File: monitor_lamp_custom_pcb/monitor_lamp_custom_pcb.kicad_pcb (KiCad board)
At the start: 2 copper layers, 50 x 35 mm, 32 parts, among them IC1 HUSB238, J1 USB_C_Receptacle_PowerOnly_6P, J2 VEML7700_Connection, J3 LD2410C_Connection, J4 Conn_01x02, J5 Conn_01x01, J7 Conn_01x01, J8 Conn_01x01, J9 Conn_01x01, Q1 AO3401A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

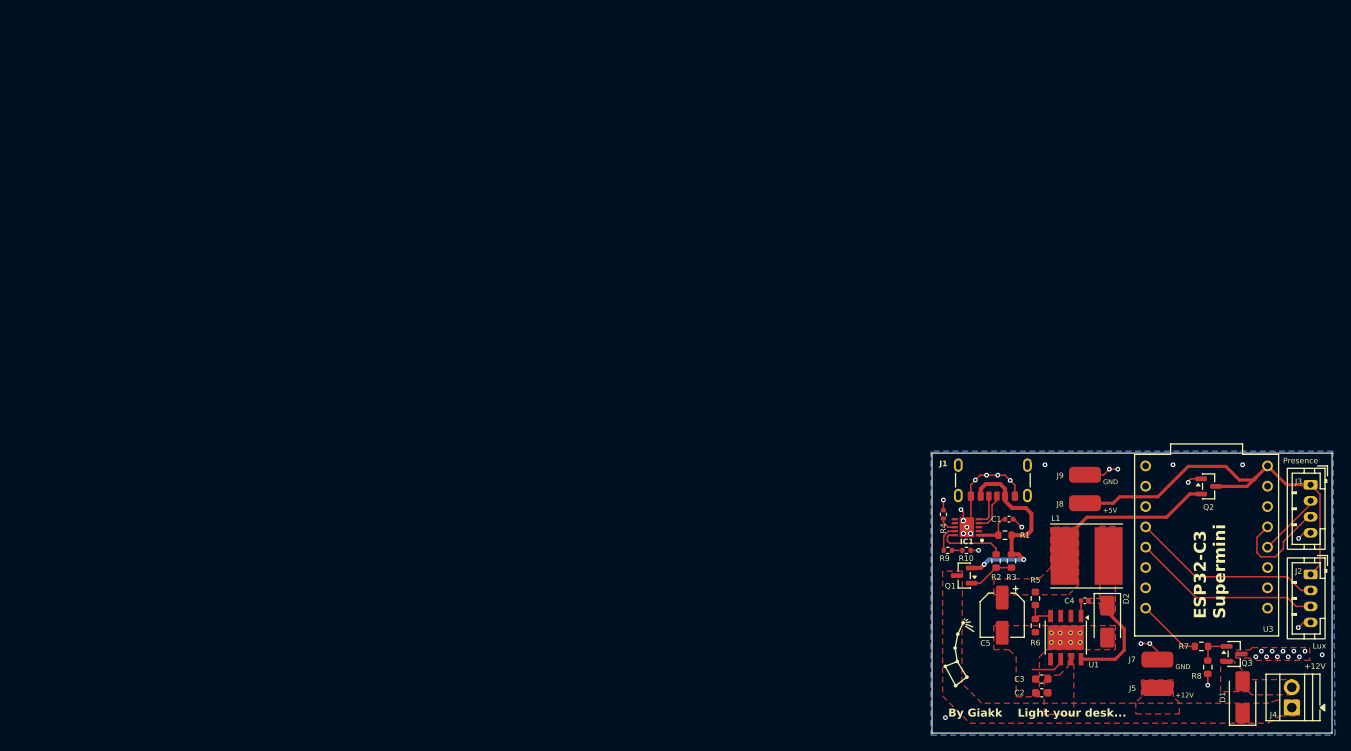
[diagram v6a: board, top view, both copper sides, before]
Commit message: Corrected ISET pin error and changed to pads for connecting LED supply
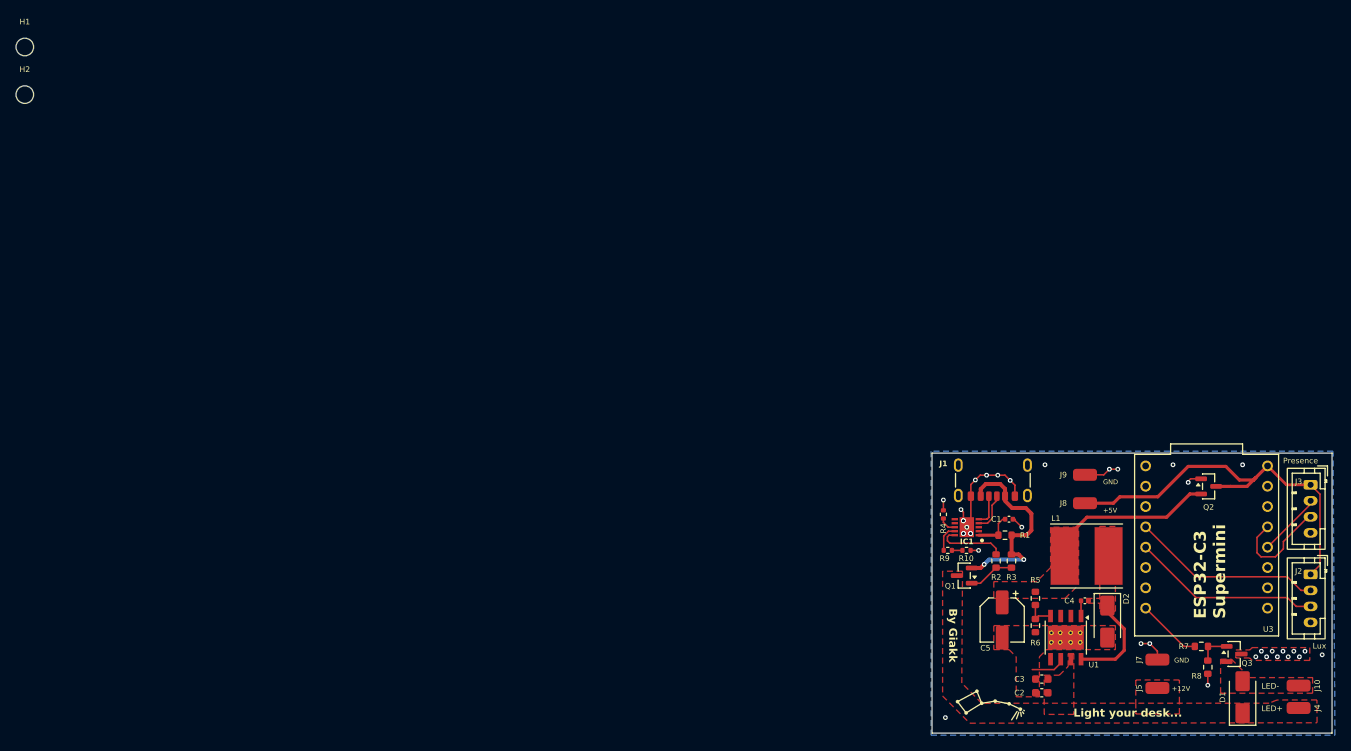
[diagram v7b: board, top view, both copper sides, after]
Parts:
- added H1: MountingHole, MountingHole:MountingHole_2.2mm_M2, F.Cu at (2.48, 2.48)
- added H2: MountingHole, MountingHole:MountingHole_2.2mm_M2, F.Cu at (2.48, 8.43)
- added J10: Conn_01x01, Connector_Wire:SolderWirePad_1x01_SMD_1.5x3mm, F.Cu at (161.7, 82.3)
- J4: value Conn_01x02 -> Conn_01x01; footprint TerminalBlock:TerminalBlock_Xinya_XY308-2.54-2P_1x02_P2.54mm_Horizontal -> Connector_Wire:SolderWirePad_1x01_SMD_1.5x3mm
- J5, J7, J8, J9: footprint Connector_Wire:SolderWirePad_1x01_SMD_2x4mm -> Connector_Wire:SolderWirePad_1x01_SMD_1.5x3mm
- moved J4 0.85 mm to (161.7, 85.1)
- moved C5 0.60 mm to (124.7, 74.1)
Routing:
- net GND: track 38.0 -> 34.4 mm, vias 38 -> 36
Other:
- board text added: "By Giakk"
- board text added: "LED+"
- board text added: "LED-"
- board text added: "Light your desk..."
- board text removed: "By Giakk Light your desk..."

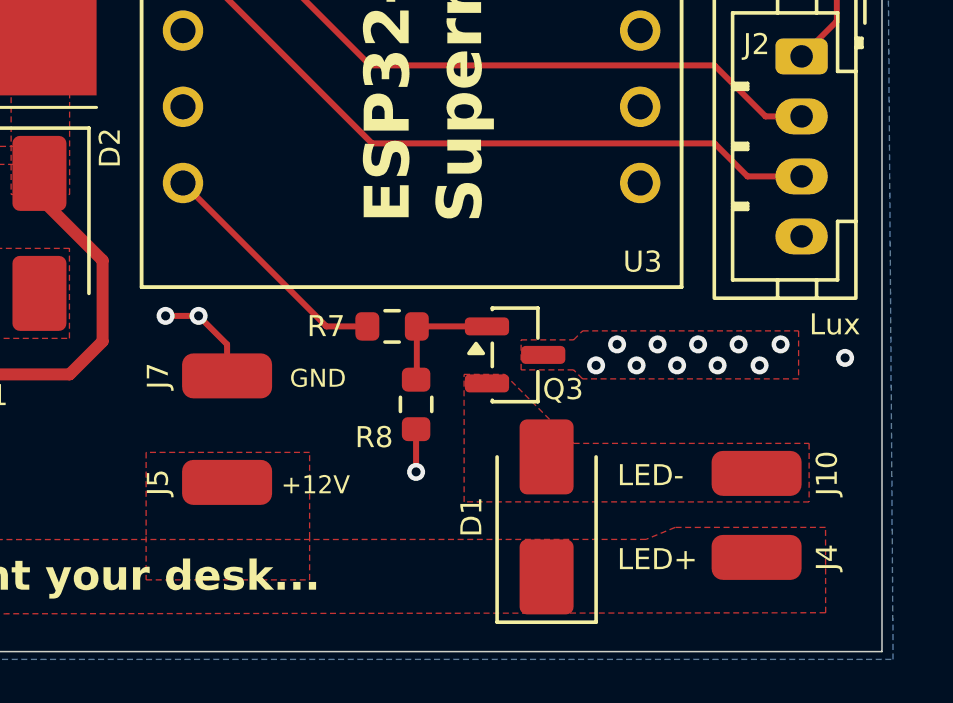
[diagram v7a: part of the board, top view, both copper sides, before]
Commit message: Corrected bug with N-Mosfet
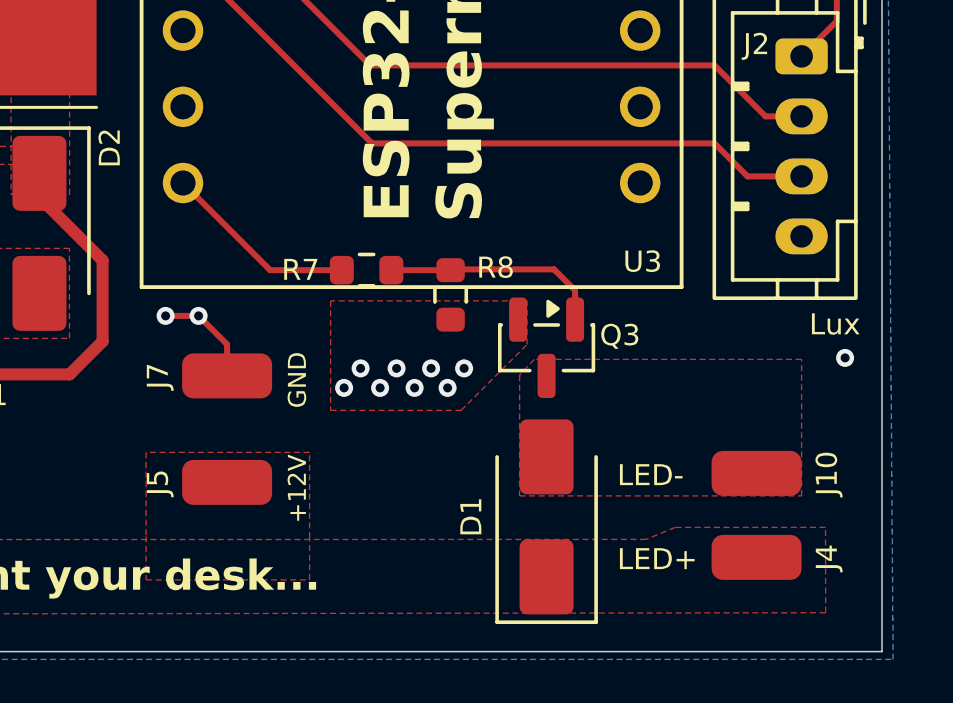
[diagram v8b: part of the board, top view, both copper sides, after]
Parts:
- moved R8 3.83 mm to (151.5, 76.3)
- moved R7 2.06 mm to (148.7, 75.5)
- moved Q3 1.08 mm to (154.7, 78.1), turned to -90 degrees
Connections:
- Q3 pad 2: Net-(D1-A) -> GND
- Q3 pad 3: GND -> Net-(D1-A)
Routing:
- net Net-(Q3-G): track 4.12 -> 7.40 mm
- net PWM_Control: track 8.12 -> 6.50 mm
- net GND: track 34.4 -> 33.0 mm, vias 36 -> 33
